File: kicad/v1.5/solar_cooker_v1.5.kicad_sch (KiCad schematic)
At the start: 12 parts, among them SW1 SW_DPST_x2, U2 microSD, U3 clock_module, U5 anemometer, U6 BME680, U7 PT100, U9 AM2315

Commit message: KiCad update
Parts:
- removed SW1: SW_DPST_x2, symbol Switch:SW_DPST_x2
- added S1: 500SSP1S2M2QEA, SW_500SSP1S2M2QEA, symbol switch:500SSP1S2M2QEA
- added U7: pyranometer, custom_components:screw_terminal_4pin, symbol custom_components:pyranometer
- D? (x2): footprint (none) -> LED_SMD:LED_1206_3216Metric_Pad1.42x1.75mm_HandSolder
- R1: footprint Resistor_SMD:R_0201_0603Metric_Pad0.64x0.40mm_HandSolder -> Resistor_SMD:R_1206_3216Metric
- R? (x2): footprint Resistor_SMD:R_0201_0603Metric_Pad0.64x0.40mm_HandSolder -> Resistor_SMD:R_1206_3216Metric_Pad1.30x1.75mm_HandSolder; Productnumber (none) -> CRGCQ1206F220R
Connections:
- net +5V: now also S1.1
- net +9V: now also U7.2 (VCC)
- net D24: now also S1.2
- net GND: now also S1.3, U7.3 (GND), U7.4 (GND)
- new net A10: U7.1 (SIG)

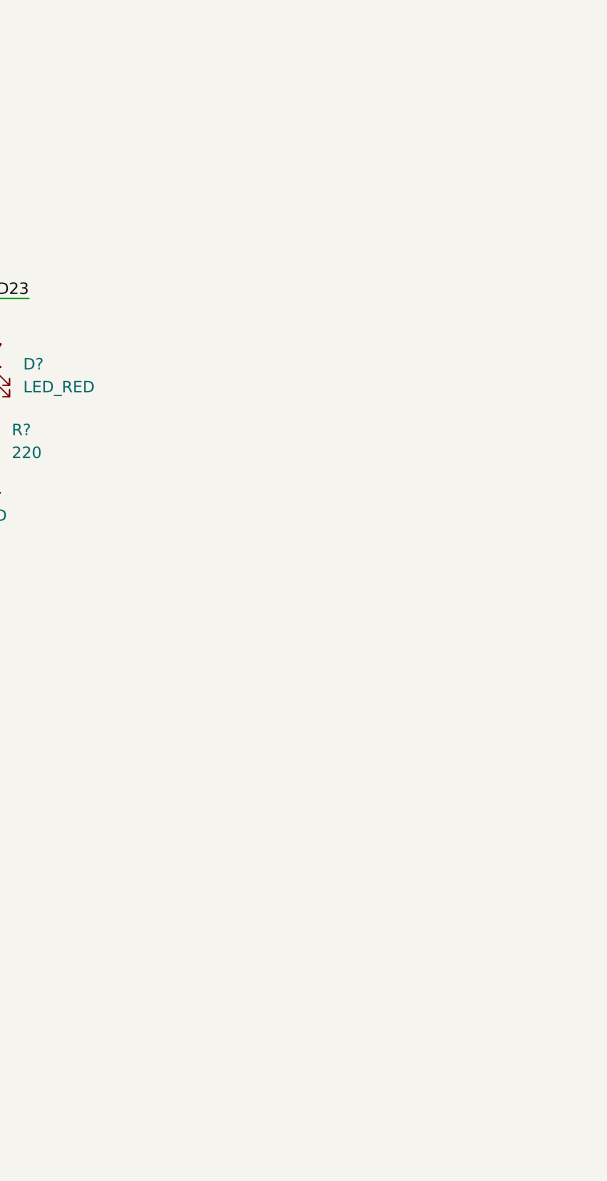
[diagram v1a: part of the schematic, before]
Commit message: added Arduino Mega KiCad
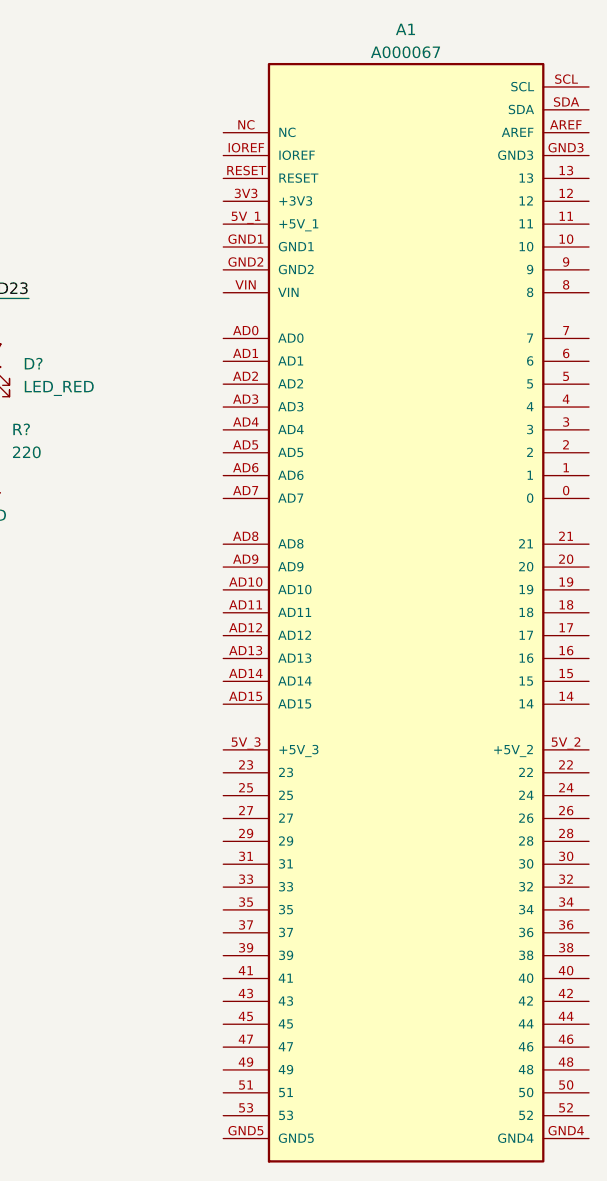
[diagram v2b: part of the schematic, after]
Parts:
- added A1: A000067, ARDUINO_A000067, symbol Arduino Mega:A000067
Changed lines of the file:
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@@
+    )
+  )
+  (symbol (lib_id "Arduino Mega:A000067") (at 244.475 87.63 0) (unit 1)
+    (in_bom yes) (on_board yes) (dnp no) (fields_autoplaced)
+    (property "Reference" "A1" (at 244.475 22.86 0)
+      (effects (font (size 1.27 1.27)))
+    )
+    (property "Value" "A000067" (at 244.475 25.4 0)
+      (effects (font (size 1.27 1.27)))
+    )
+    (property "Footprint" "ARDUINO_A000067" (at 244.475 87.63 0)
+      (effects (font (size 1.27 1.27)) (justify bottom) hide)
+    )
+    (property "Datasheet" "" (at 244.475 87.63 0)
+      (effects (font (size 1.27 1.27)) hide)
+    )
+    (property "MF" "Arduino" (at 244.475 87.63 0)
+      (effects (font (size 1.27 1.27)) (justify bottom) hide)
+    )
+    (property "DESCRIPTION" "Dev.kit: Arduino; SPI, TWI, UART; ICSP, USB B, pin strips, supply" (at 244.475 87.63 0)
+      (effects (font (size 1.27 1.27)) (justify bottom) hide)
+    )
+    (property "PACKAGE" "None" (at 244.475 87.63 0)
+      (effects (font (size 1.27 1.27)) (justify bottom) hide)
+    )
+    (property "PRICE" "None" (at 244.475 87.63 0)
+      (effects (font (size 1.27 1.27)) (justify bottom) hide)
+    )
+    (property "MP" "ARDUINO MEGA2560 REV3 - RETAIL" (at 244.475 87.63 0)
+      (effects (font (size 1.27 1.27)) (justify bottom) hide)
+    )
+    (property "AVAILABILITY" "Unavailable" (at 244.475 87.63 0)
+      (effects (font (size 1.27 1.27)) (justify bottom) hide)
+    )
+    (pin "0")
+    (pin "1")
+    (pin "10")
+    (pin "11")
+    (pin "12")
+    (pin "13")
+    (pin "14")
+    (pin "15")
+    (pin "16")
+    (pin "17")
+    (pin "18")
+    (pin "19")
+    (pin "2")
+    (pin "20")
+    (pin "21")
+    (pin "22")
+    (pin "23")
+    (pin "24")
+    (pin "25")
+    (pin "26")
+    (pin "27")
+    (pin "28")
+    (pin "29")
+    (pin "3")
+    (pin "30")
+    (pin "31")
+    (pin "32")
+    (pin "33")
+    (pin "34")
+    (pin "35")
+    (pin "36")
+    (pin "37")
+    (pin "38")
+    (pin "39")
+    (pin "3V3")
+    (pin "4")
+    (pin "40")
+    (pin "41")
+    (pin "42")
+    (pin "43")
+    (pin "44")
+    (pin "45")
+    (pin "46")
+    (pin "47")
+    (pin "48")
+    (pin "49")
+    (pin "5")
+    (pin "50")
+    (pin "51")
+    (pin "52")
+    (pin "53")
+    (pin "5V_1")
+    (pin "5V_2")
+    (pin "5V_3")
+    (pin "6")
+    (pin "7")
+    (pin "8")
+    (pin "9")
+    (pin "AD0")
+    (pin "AD1")
+    (pin "AD10")
+    (pin "AD11")
+    (pin "AD12")
+    (pin "AD13")
+    (pin "AD14")
+    (pin "AD15")
+    (pin "AD2")
+    (pin "AD3")
+    (pin "AD4")
+    (pin "AD5")
+    (pin "AD6")
+    (pin "AD7")
+    (pin "AD8")
+    (pin "AD9")
+    (pin "AREF")
+    (pin "GND1")
+    (pin "GND2")
+    (pin "GND3")
+    (pin "GND4")
+    (pin "GND5")
+    (pin "IOREF")
+    (pin "NC")
+    (pin "RESET")
+    (pin "SCL")
+    (pin "SDA")
+    (pin "VIN")
+    (instances
+      (project "solar_cooker_v1.5"
+        (path "/c2c342ae-c172-4b44-a50e-ddd387eb2591"
+          (reference "A1") (unit 1)
+        )
+      )
     )
   )

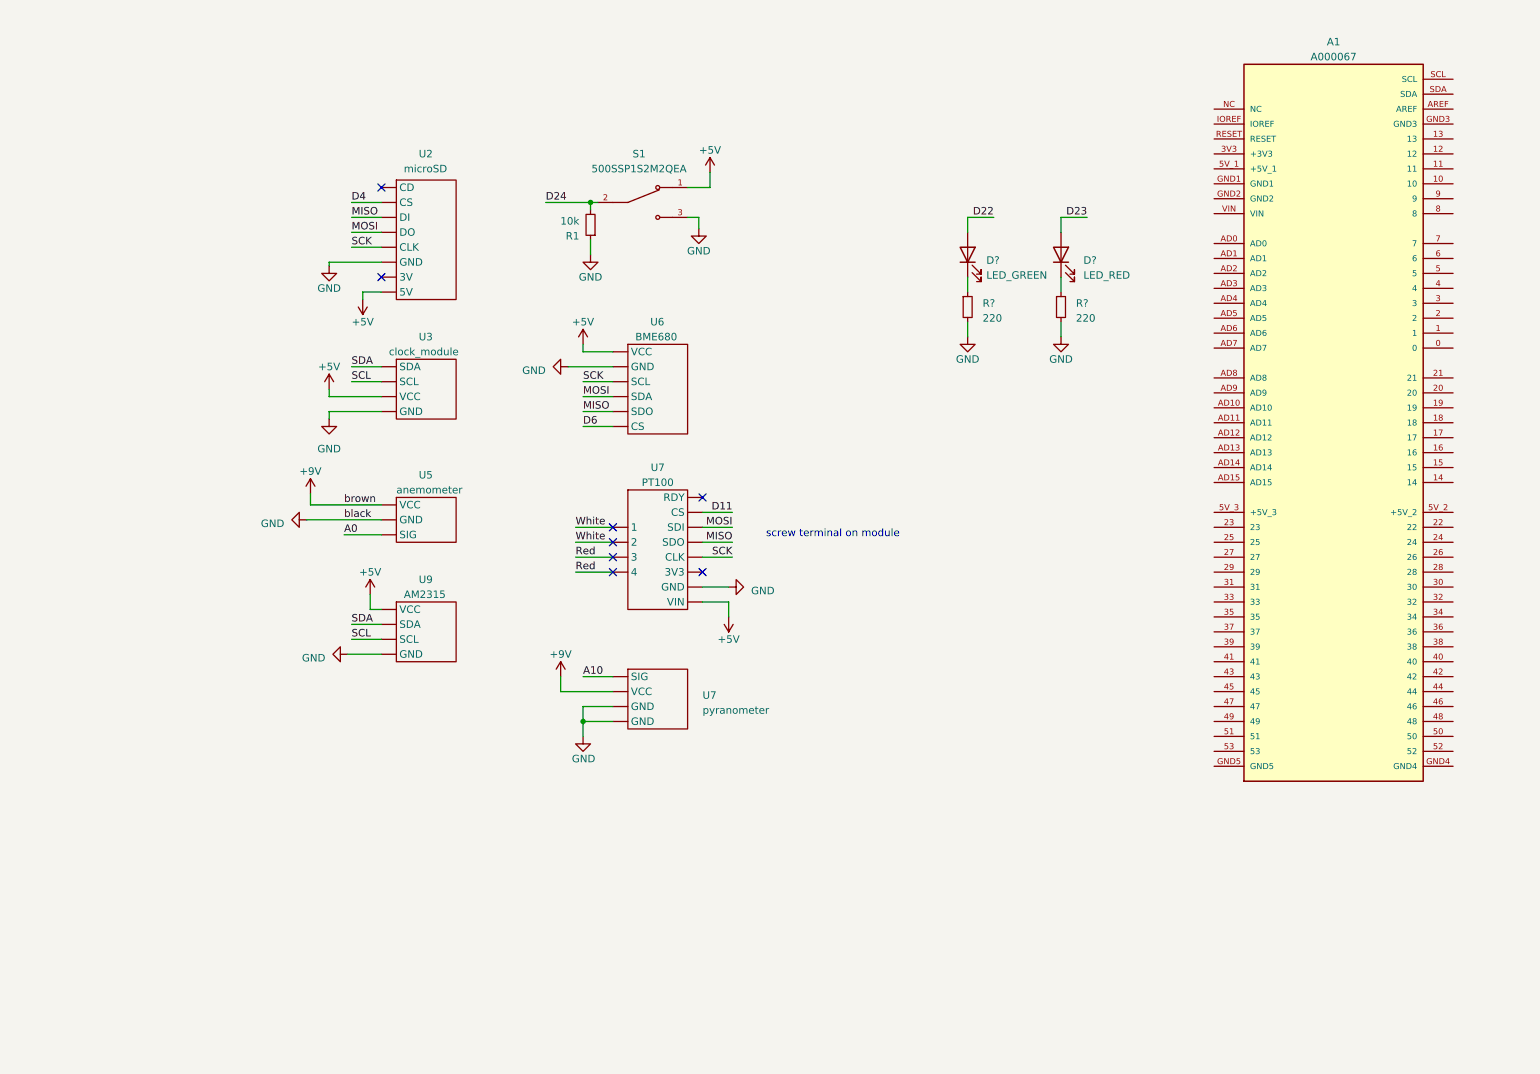
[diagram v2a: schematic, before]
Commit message: pcb has now 3 pt100 sensors
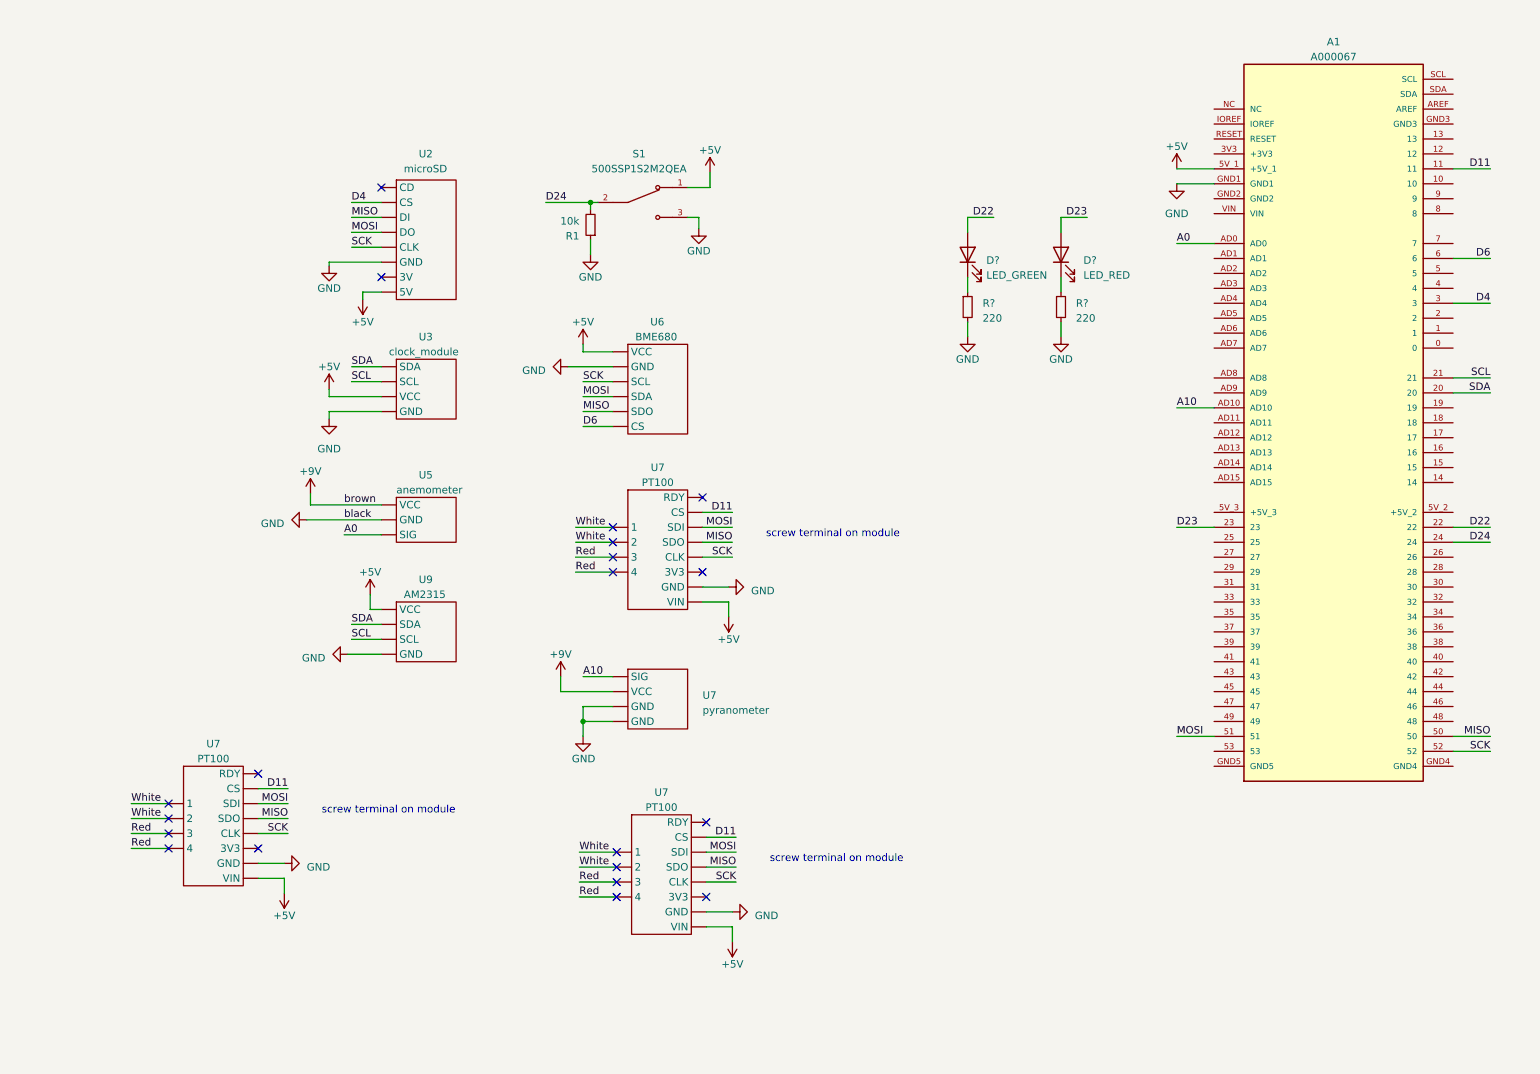
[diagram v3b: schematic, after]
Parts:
- added U7 (x2): PT100, custom_components:PT100, symbol custom_components:temperature_inside_pot
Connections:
- net +5V: now also A1.5V_1 (+5V_1), U7.12 (VIN), U7.12 (VIN)
- net A0: now also A1.AD0
- net A10: now also A1.AD10
- net D11: now also A1.11, U7.6 (CS), U7.6 (CS)
- net D22: now also A1.22
- net D23: now also A1.23
- net D24: now also A1.24
- net D4: now also A1.3
- net D6: now also A1.6
- net GND: now also A1.GND1, U7.11 (GND), U7.11 (GND)
- net MISO: now also A1.50, U7.8 (SDO), U7.8 (SDO)
- net MOSI: now also A1.51, U7.7 (SDI), U7.7 (SDI)
- net Red: now also U7.3, U7.3, U7.4, U7.4
- net SCK: now also A1.52, U7.9 (CLK), U7.9 (CLK)
- net SCL: now also A1.21
- net SDA: now also A1.20
- net White: now also U7.1, U7.1, U7.2, U7.2
- no-connect marks 8 -> 20

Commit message: added GPS to pcb
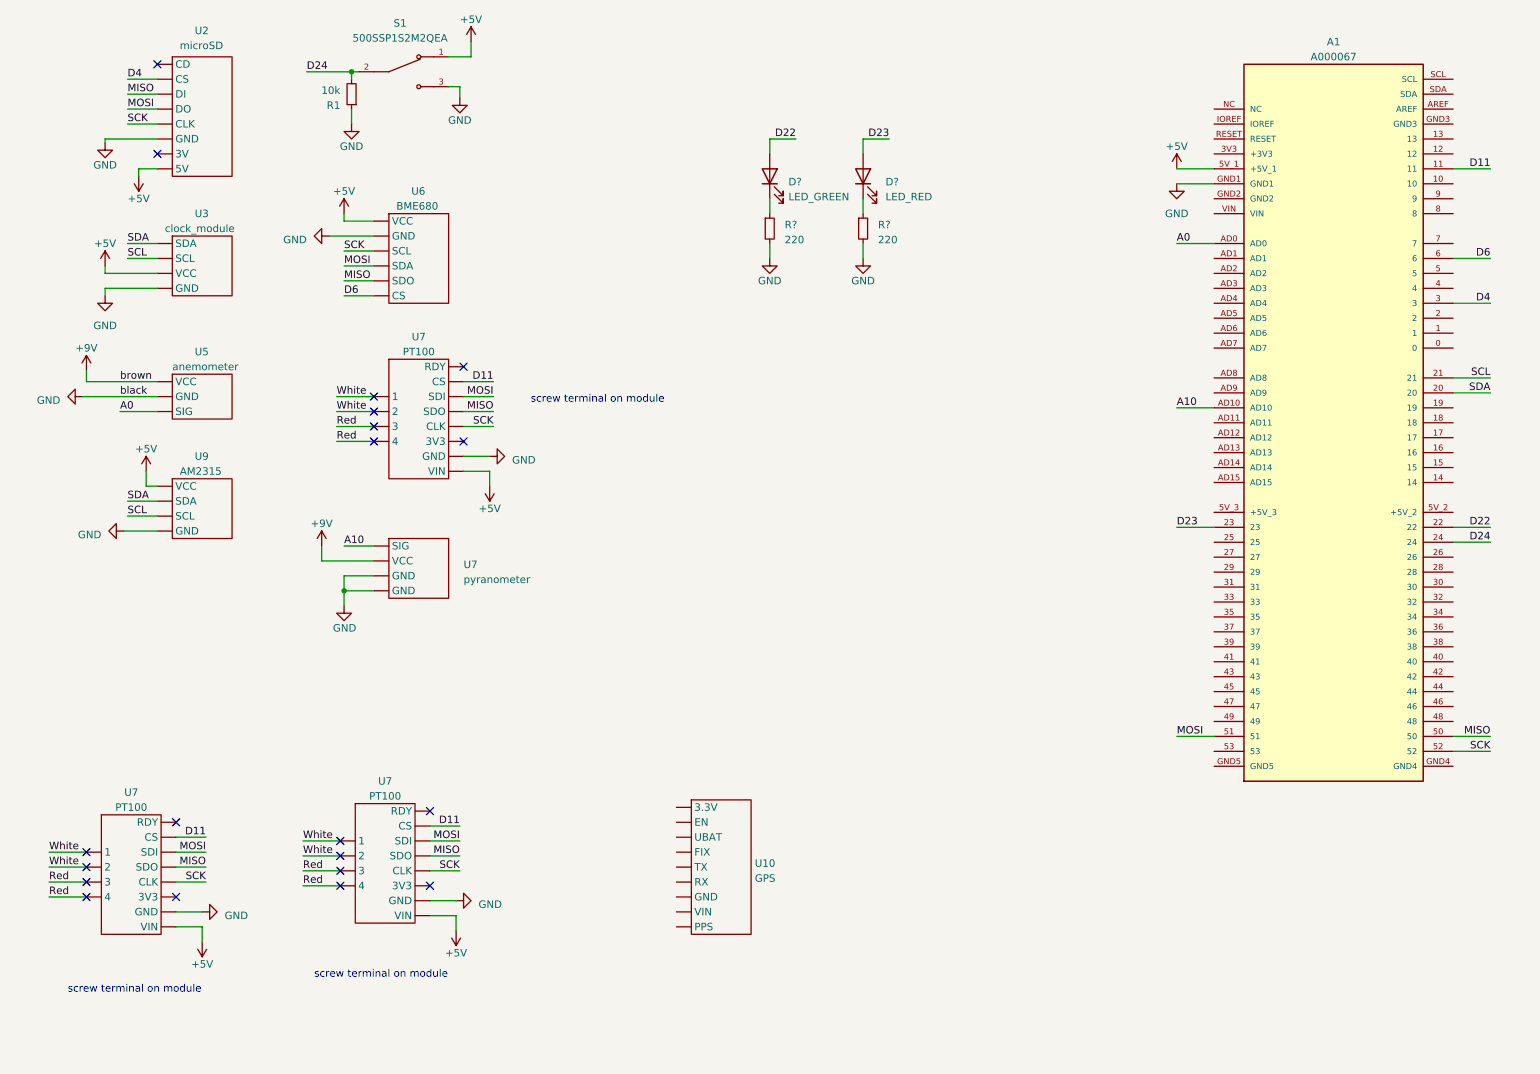
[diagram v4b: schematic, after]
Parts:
- added U10: GPS, custom_components:GPS, symbol custom_components:GPS
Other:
- moved on the sheet: D?, R1, R?, S1, U2, U3, U5, U6, U7, U9

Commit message: routing update
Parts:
- removed U7 (x3): PT100, custom_components:PT100, symbol custom_components:temperature_inside_pot
- added U6, U8, U9: PT100, custom_components:PT100, symbol custom_components:PT100
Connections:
- net +5V: now also U6.8 (VIN), U8.8 (VIN), U9.8 (VIN)
- net D11: now also U6.2 (CS)
- net GND: now also U6.7 (GND), U8.7 (GND), U9.7 (GND)
- net MISO: now also U6.4 (SDO), U8.4 (SDO), U9.4 (SDO)
- net MOSI: now also U6.3 (SDI), U8.3 (SDI), U9.3 (SDI)
- net SCK: now also U6.5 (CLK), U8.5 (CLK), U9.5 (CLK)
- net D12: now reaches A1.12
- net D12: now also U8.2 (CS)
- net D13: now reaches A1.13
- net D13: now also U9.2 (CS)
- no-connect marks 20 -> 8
